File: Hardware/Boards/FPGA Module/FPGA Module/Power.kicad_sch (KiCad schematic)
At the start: 115 parts, among them Q2 IRLML6244, Q3 IRLML6244, Q4 IRLML6244, Q5 IRLML6244, Q6 IRLML6244, U10 INA700AYWFR, U12 INA700AYWFR, U13 L78L05_SOT89, U2 INA700AYWFR, U22 TPSM33625RDNR, U23 TPSM33625RDNR, U24 TPSM33625RDNR, U3 AOZ2369QI-11, U4 TPS62933O, U7 INA700AYWFR, U8 INA236

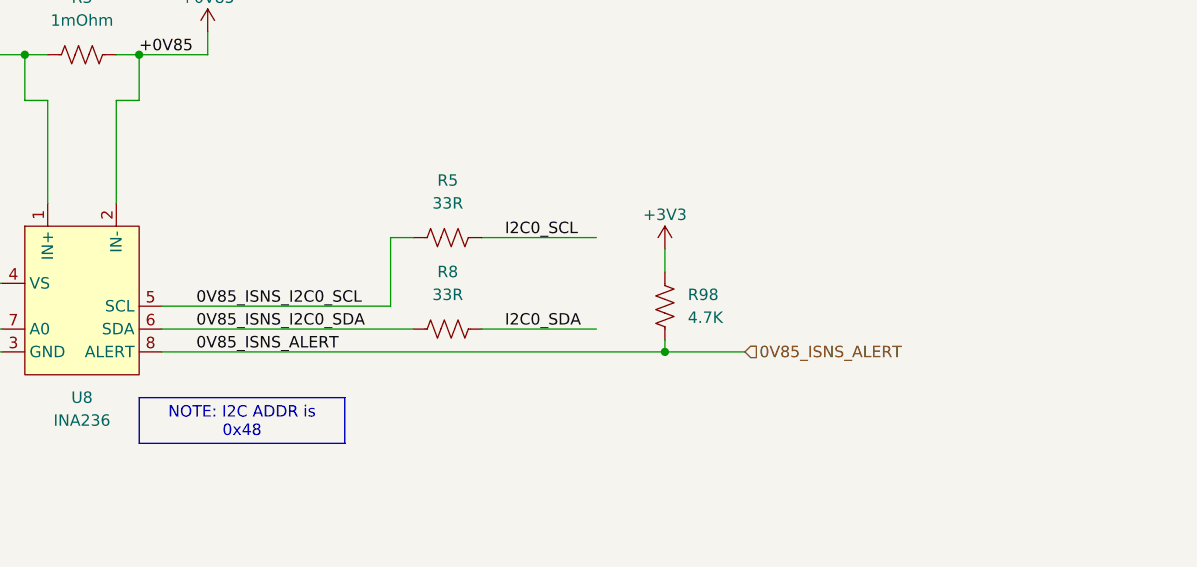
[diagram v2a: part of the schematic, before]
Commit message: Added Top sheet connections for FPGA module
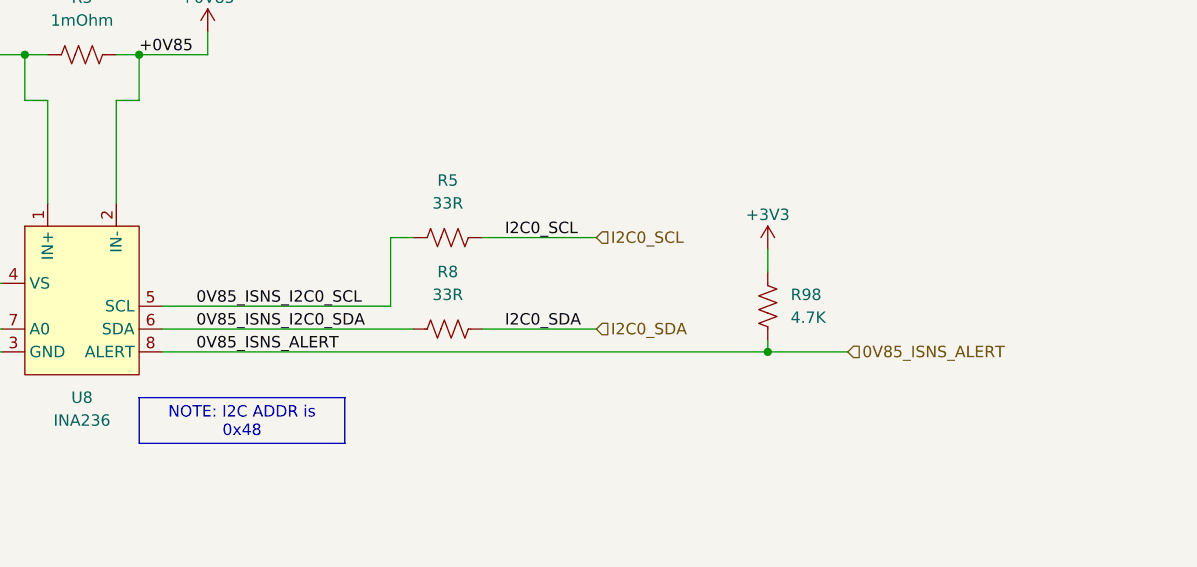
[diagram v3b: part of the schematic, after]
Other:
- moved on the sheet: R98
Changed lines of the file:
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@@
 	)
 	(junction
+		(at 375.92 74.93)
+		(diameter 0)
+		(color 0 0 0 0)
+	)
+	(junction
 		(at 210.82 331.47)
 		(diameter 0)
@@
 	)
 	(junction
-		(at 364.49 74.93)
-		(diameter 0)
-		(color 0 0 0 0)
-	)
-	(junction
 		(at 293.37 41.91)
 		(diameter 0)
@@
 	(wire
 		(pts
+			(xy 375.92 74.93) (xy 384.81 74.93)
+		)
+		(stroke
+			(width 0)
+			(type default)
+		)
+	)
+	(wire
+		(pts
 			(xy 189.23 349.25) (xy 189.23 358.14)
 		)
@@
 	(wire
 		(pts
-			(xy 308.61 74.93) (xy 364.49 74.93)
+			(xy 308.61 74.93) (xy 375.92 74.93)
 		)
 		(stroke
@@
 	(wire
 		(pts
-			(xy 364.49 63.5) (xy 364.49 66.04)
+			(xy 375.92 63.5) (xy 375.92 66.04)
 		)
 		(stroke
@@
 	(wire
 		(pts
-			(xy 364.49 73.66) (xy 364.49 74.93)
+			(xy 375.92 73.66) (xy 375.92 74.93)
 		)
 		(stroke
@@
 	(wire
 		(pts
-			(xy 364.49 74.93) (xy 373.38 74.93)
-		)
-		(stroke
-			(width 0)
-			(type default)
-		)
-	)
-	(wire
-		(pts
 			(xy 185.42 214.63) (xy 185.42 215.9)
 		)
@@
 		)
 	)
+	(hierarchical_label "I2C0_SCL"
+		(shape input)
+		(at 356.87 62.23 0)
+		(fields_autoplaced yes)
+		(effects
+			(font
+				(size 1.27 1.27)
+			)
+			(justify left)
+		)
+	)
 	(hierarchical_label "1V8_ISNS_ALERT"
 		(shape input)
@@
 		)
 	)
+	(hierarchical_label "I2C0_SDA"
+		(shape input)
+		(at 356.87 72.39 0)
+		(fields_autoplaced yes)
+		(effects
+			(font
+				(size 1.27 1.27)
+			)
+			(justify left)
+		)
+	)
 	(hierarchical_label "1V2_ISNS_ALERT"
 		(shape input)
@@
 	(hierarchical_label "0V85_ISNS_ALERT"
 		(shape input)
-		(at 373.38 74.93 0)
+		(at 384.81 74.93 0)
 		(fields_autoplaced yes)
 		(effects
@@
 	(symbol
 		(lib_id "Device:R_US")
-		(at 364.49 69.85 180)
+		(at 375.92 69.85 180)
 		(unit 1)
 		(exclude_from_sim no)
@@
 		(fields_autoplaced yes)
 		(property "Reference" "R98"
-			(at 367.03 68.5799 0)
+			(at 378.46 68.5799 0)
 			(effects
 				(font
@@
 		)
 		(property "Value" "4.7K"
-			(at 367.03 71.1199 0)
+			(at 378.46 71.1199 0)
 			(effects
 				(font
@@
 		)
 		(property "Footprint" "Resistor_SMD:R_0402_1005Metric"
-			(at 363.474 69.596 90)
+			(at 374.904 69.596 90)
 			(effects
 				(font
@@
 		)
 		(property "Datasheet" "~"
-			(at 364.49 69.85 0)
+			(at 375.92 69.85 0)
 			(effects
 				(font
@@
 		)
 		(property "Description" "Resistor, US symbol"
-			(at 364.49 69.85 0)
+			(at 375.92 69.85 0)
 			(effects
 				(font
@@
 	(symbol
 		(lib_id "power:+3V3")
-		(at 364.49 63.5 0)
+		(at 375.92 63.5 0)
 		(unit 1)
 		(exclude_from_sim no)
@@
 		(dnp no)
 		(property "Reference" "#PWR032"
-			(at 364.49 67.31 0)
+			(at 375.92 67.31 0)
 			(effects
 				(font
@@
 		)
 		(property "Value" "+3V3"
-			(at 364.49 59.69 0)
+			(at 375.92 59.69 0)
 			(effects
 				(font
@@
 		)
 		(property "Footprint" ""
-			(at 364.49 63.5 0)
+			(at 375.92 63.5 0)
 			(effects
 				(font
@@
 		)
 		(property "Datasheet" ""
-			(at 364.49 63.5 0)
+			(at 375.92 63.5 0)
 			(effects
 				(font
@@
 		)
 		(property "Description" "Power symbol creates a global label with name \"+3V3\""
-			(at 364.49 63.5 0)
+			(at 375.92 63.5 0)
 			(effects
 				(font

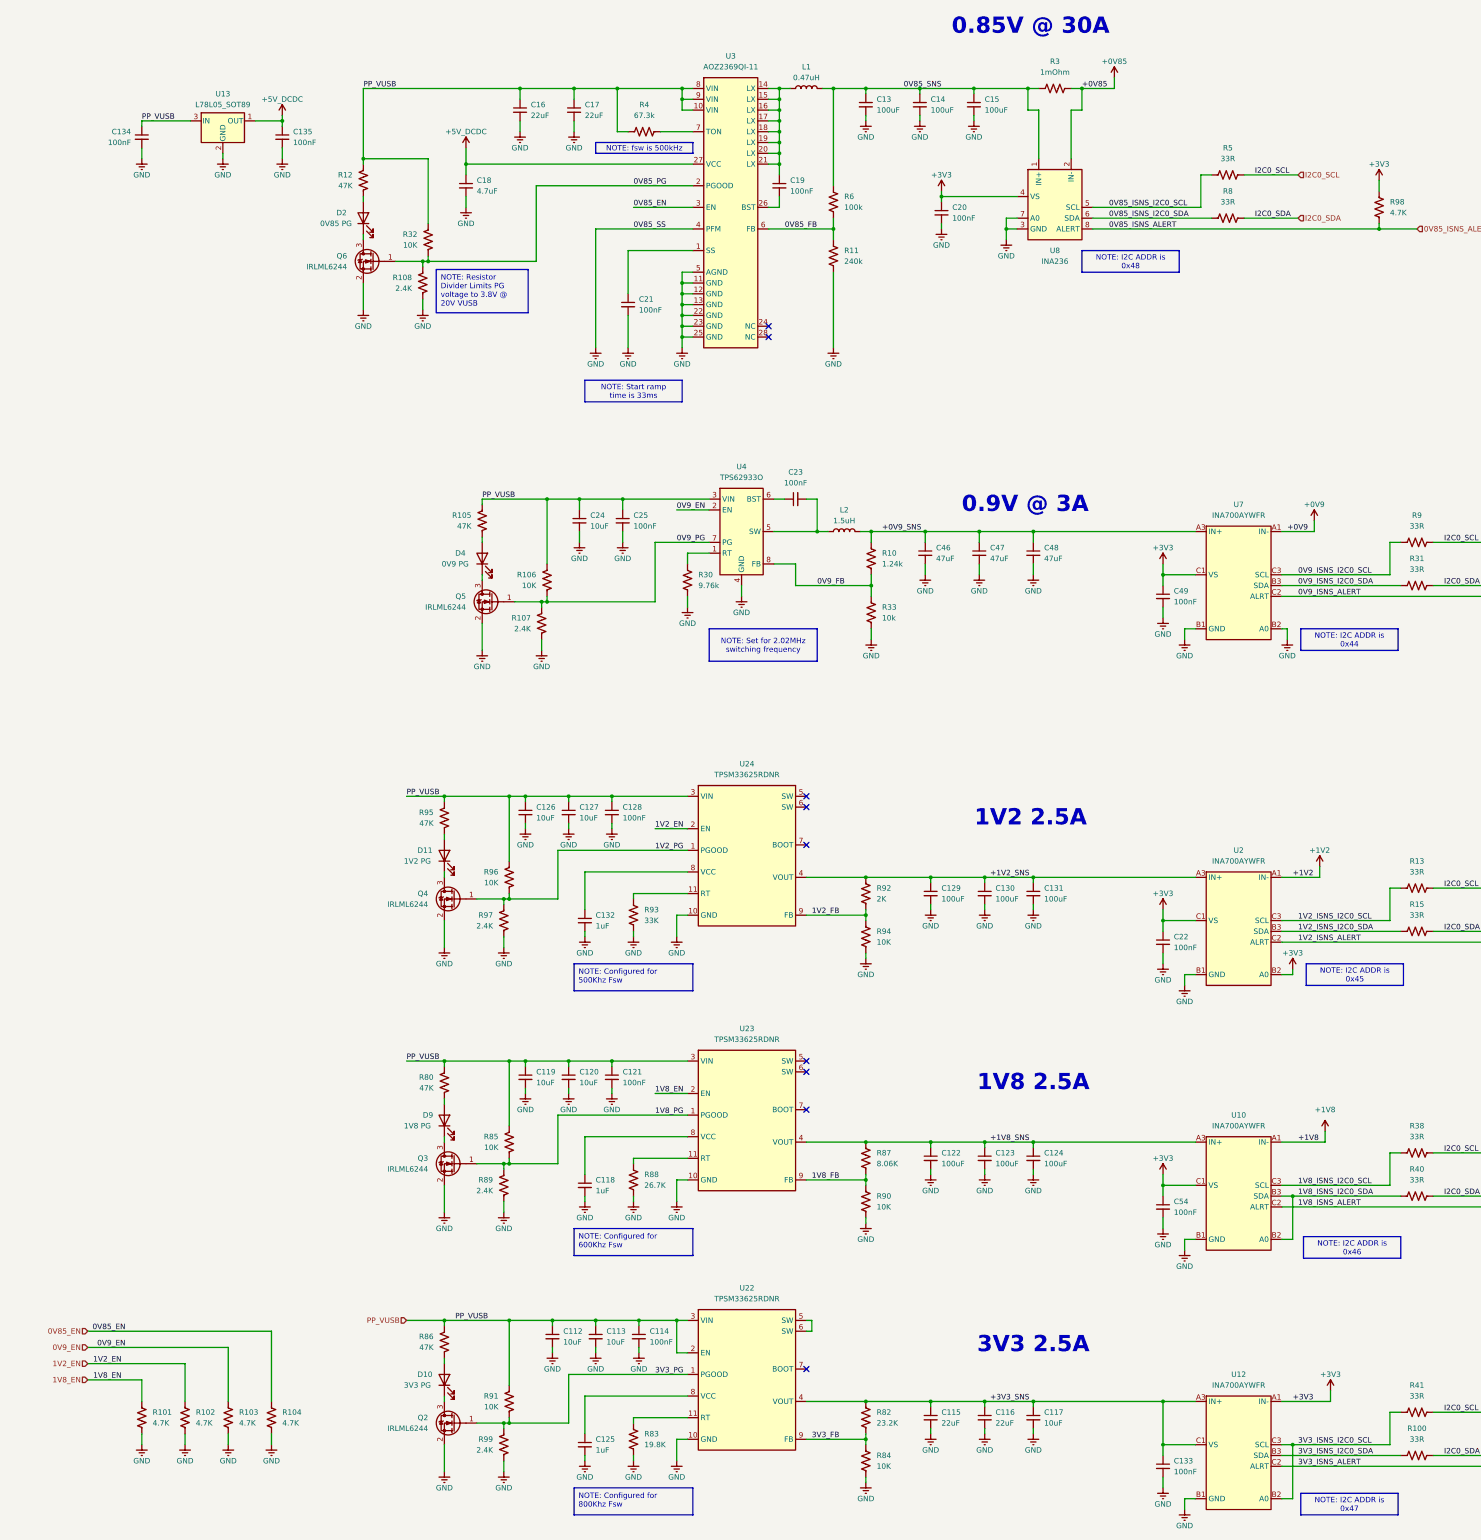
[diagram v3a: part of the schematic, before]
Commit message: FPGA Module sch update
Added 3V3 LDO for MCU and 3V3 EN for DCDC. Also added SPI bus from MCU to FPGA with level shifter
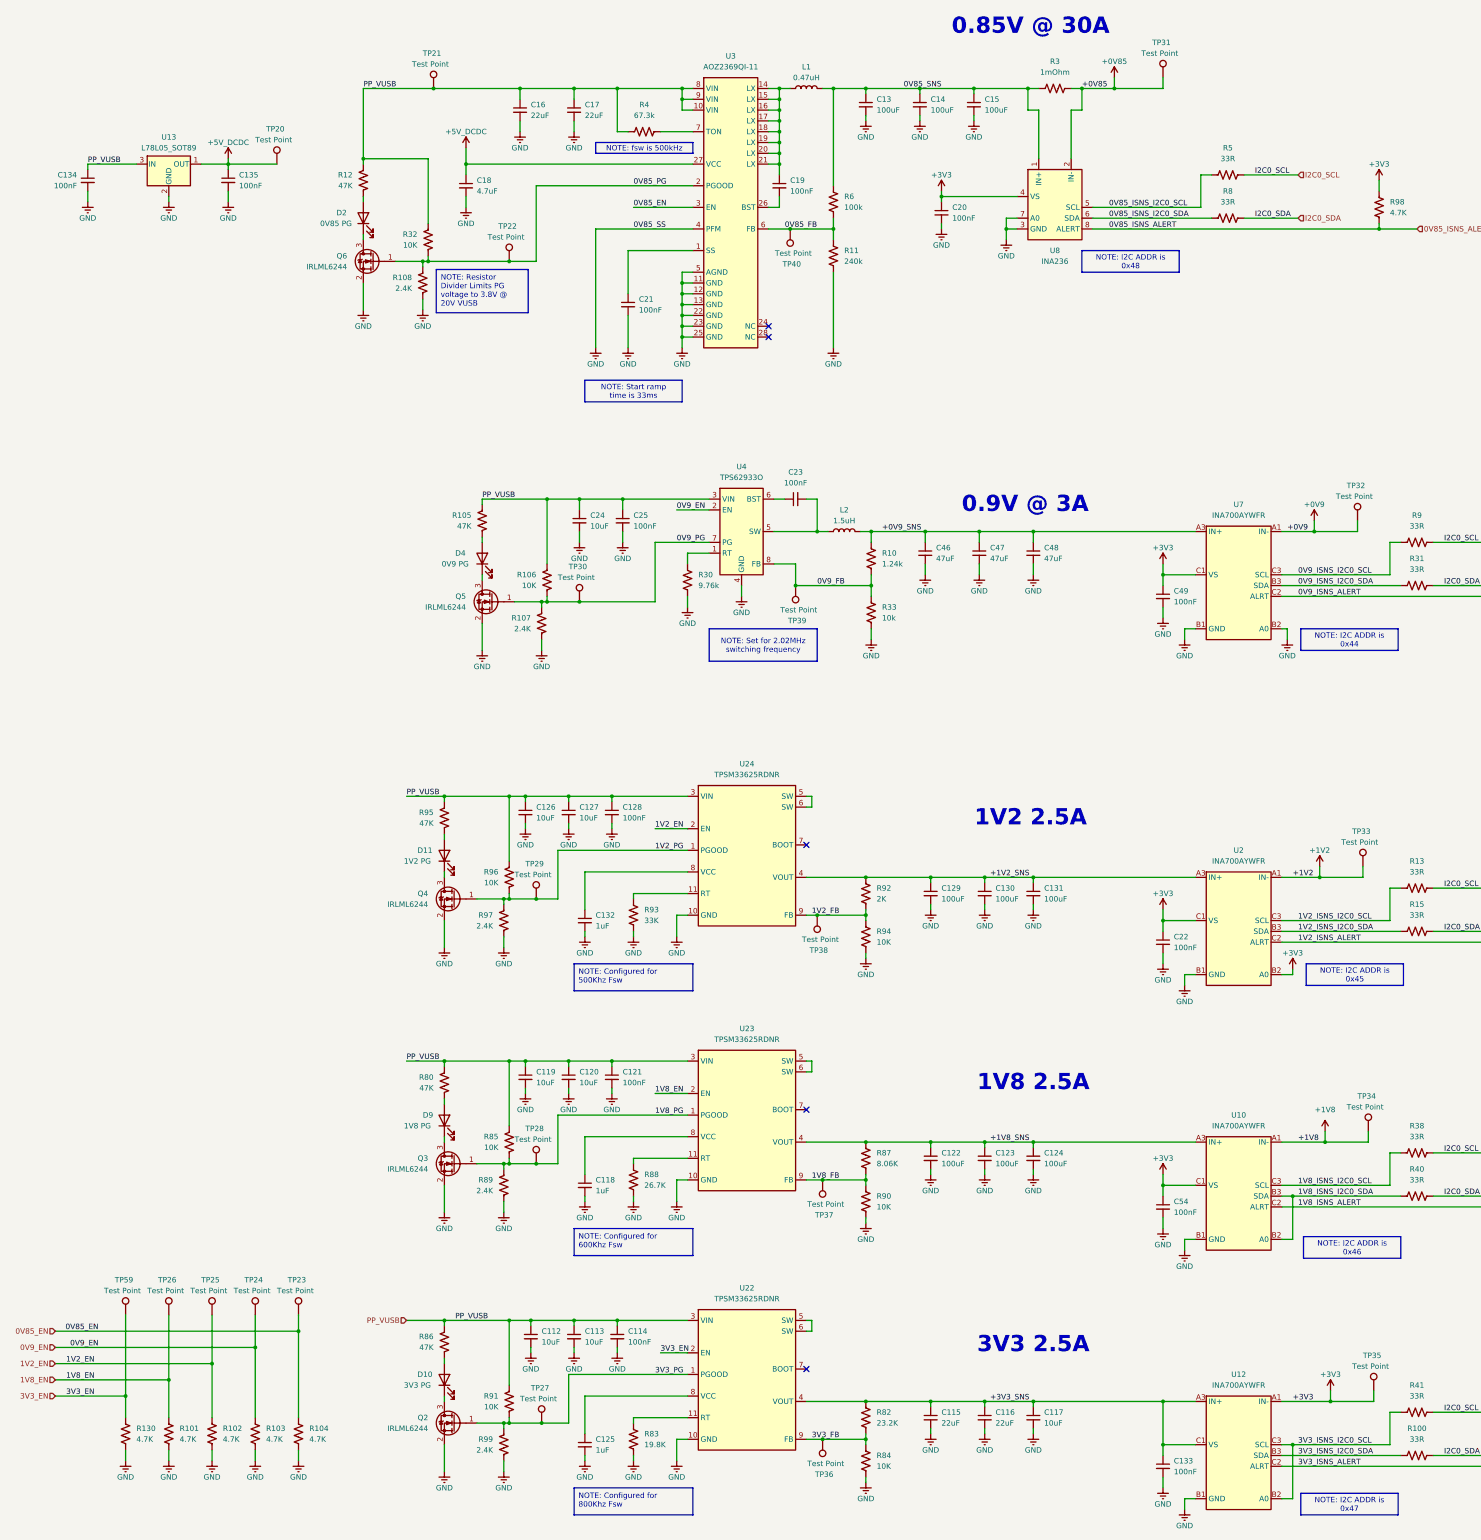
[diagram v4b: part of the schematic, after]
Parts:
- added R130: 4.7K, Resistor_SMD:R_0402_1005Metric, symbol Device:R_US
- added TP20, TP21, TP22, TP23, TP24, TP25, TP26, TP27, TP28, TP29, TP30, TP31, TP32, TP33, TP34, TP35, TP36, TP37, TP38, TP39, TP40, TP59: Test Point, FPGA Module:Test Point 0.75mm, symbol Connector:TestPoint
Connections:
- net +0V85: now also TP31.1
- net +0V9: now also TP32.1
- net +1V2: now also TP33.1
- net +1V8: now also TP34.1
- net +3V3: now also TP35.1
- net +5V_DCDC: now also TP20.1
- net 0V85_EN: now also TP23.1
- net 0V85_FB: now also TP40.1
- net 0V85_PG: now also TP22.1
- net 0V9_EN: now also TP24.1
- net 0V9_FB: now also TP39.1
- net 0V9_PG: now also TP30.1
- net 1V2_EN: now also TP25.1
- net 1V2_FB: now also TP38.1
- net 1V2_PG: now also TP29.1
- net 1V8_EN: now also TP26.1
- net 1V8_FB: now also TP37.1
- net 1V8_PG: now also TP28.1
- net 3V3_FB: now also TP36.1
- net 3V3_PG: now also TP27.1
- net GND: now also R130.1
- net PP_VUSB: now also TP21.1; no longer U22.2 (EN)
- net at U24.5 (SW): now also U24.6 (SW)
- net at U23.5 (SW): now also U23.6 (SW)
- new net 3V3_EN: R130.2, TP59.1, U22.2 (EN)
- no-connect marks 9 -> 5
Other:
- moved on the sheet: C112, C113, C114, C134, C135, R101, R102, R103, R104, U13

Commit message: Completed FPGA module PCB layout
Started PCB routing
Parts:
- removed C112, C113, C117, C119, C120, C126, C127, C24: 10uF, Capacitor_SMD:C_0603_1608Metric, symbol Device:C_Small
- removed C114, C121, C128: 100nF, Capacitor_SMD:C_0201_0603Metric, symbol Device:C_Small
- removed C115, C116, C16, C17: 22uF, Capacitor_SMD:C_0805_2012Metric, symbol Device:C_Small
- removed C118, C125, C132: 1uF, Capacitor_SMD:C_0402_1005Metric, symbol Device:C_Small
- removed C122, C123, C124, C129, C13, C130, C131, C14, C15: 100uF, Capacitor_SMD:C_0805_2012Metric, symbol Device:C_Small
- removed C134, C135, C19, C21, C23, C25: 100nF, Capacitor_SMD:C_0402_1005Metric, symbol Device:C_Small
- removed C18: 4.7uF, Capacitor_SMD:C_0402_1005Metric, symbol Device:C_Small
- removed C46, C47, C48: 47uF, Capacitor_SMD:C_0603_1608Metric, symbol Device:C_Small
- removed D2: 0V85 PG, LED_SMD:LED_0603_1608Metric, symbol Device:LED
- removed D4: 0V9 PG, LED_SMD:LED_0603_1608Metric, symbol Device:LED
- removed Q2, Q3, Q4, Q5, Q6: IRLML6244, Package_TO_SOT_SMD:SOT-23, symbol Transistor_FET:IRLML6244
- removed R10: 1.24k, Resistor_SMD:R_0402_1005Metric, symbol Device:R_US
- removed R105, R12, R80, R86, R95: 47K, Resistor_SMD:R_0402_1005Metric, symbol Device:R_US
- removed R106, R32, R84, R90, R91, R96: 10K, Resistor_SMD:R_0402_1005Metric, symbol Device:R_US
- removed R107, R108, R89, R97, R99: 2.4K, Resistor_SMD:R_0402_1005Metric, symbol Device:R_US
- removed R11: 240k, Resistor_SMD:R_0402_1005Metric, symbol Device:R_US
- removed R30: 9.76k, Resistor_SMD:R_0402_1005Metric, symbol Device:R_US
- removed R33: 10k, Resistor_SMD:R_0402_1005Metric, symbol Device:R_US
- removed R4: 67.3k, Resistor_SMD:R_0402_1005Metric, symbol Device:R_US
- removed R6: 100k, Resistor_SMD:R_0402_1005Metric, symbol Device:R_US
- removed R82: 23.2K, Resistor_SMD:R_0402_1005Metric, symbol Device:R_US
- removed R83: 19.8K, Resistor_SMD:R_0402_1005Metric, symbol Device:R_US
- removed R87: 8.06K, Resistor_SMD:R_0402_1005Metric, symbol Device:R_US
- removed R88: 26.7K, Resistor_SMD:R_0402_1005Metric, symbol Device:R_US
- removed R92: 2K, Resistor_SMD:R_0402_1005Metric, symbol Device:R_US
- removed R93: 33K, Resistor_SMD:R_0402_1005Metric, symbol Device:R_US
- removed TP20, TP21, TP22, TP27, TP28, TP29, TP30, TP36, TP37, TP38, TP39, TP40: Test Point, FPGA Module:Test Point 0.75mm, symbol Connector:TestPoint
- removed U13: L78L05_SOT89, Package_TO_SOT_SMD:SOT-89-3, symbol Regulator_Linear:L78L05_SOT89
- removed U22, U23, U24: TPSM33625RDNR, IO_Module:RDN0011A-MFG, symbol IO_Module:TPSM33625
- removed U3: AOZ2369QI-11, FPGA Module:AOZ2369QI11, symbol FPGA Module:AOZ2369QI-11
- removed U4: TPS62933O, Package_TO_SOT_SMD:SOT-583-8, symbol Regulator_Switching:TPS62933O
- added C140, C141, C142, C143: 1nF, Capacitor_SMD:C_0201_0603Metric, symbol Device:C_Small
- added C144, C145, C166, C169, C170, C171, C172, C173: 47uF, Capacitor_SMD:C_0603_1608Metric, symbol Device:C_Small
- added C146, C147, C148, C161, C162, C163, C77, C78, C79, C80, C81, C82, C83, C84: 22uF, Capacitor_SMD:C_0805_2012Metric, symbol Device:C_Small
- added C149, C164, C174, C175, C176, C177: 100nF, Capacitor_SMD:C_0201_0603Metric, symbol Device:C_Small
- added C150, C160, C165: 220nF, Capacitor_SMD:C_0201_0603Metric, symbol Device:C_Small
- added C151: 2.2nF, Capacitor_SMD:C_0402_1005Metric, symbol Device:C_Small
- added C152, C153, C154, C157: 100uF, Capacitor_SMD:C_0805_2012Metric, symbol Device:C_Small
- added C155, C156: 560uF, Capacitor_Tantalum_SMD:CP_EIA-7343-31_Kemet-D, symbol Device:C_Polarized_Small_US
- added C158, C159, C167, C168: 4.7uF, Capacitor_SMD:C_0201_0603Metric, symbol Device:C_Small
- added C178, C180, C182, C184: 4.7pF, Capacitor_SMD:C_0201_0603Metric, symbol Device:C_Small
- added C179, C181, C183, C185: 220pF, Capacitor_SMD:C_0201_0603Metric, symbol Device:C_Small
- added C186, C91: 10uF, Capacitor_SMD:C_0603_1608Metric, symbol Device:C_Small
- added C73, C85, C88, C89, C90: 1uF, Capacitor_SMD:C_0402_1005Metric, symbol Device:C_Small
- added C87, C92: 4.7uF, Capacitor_SMD:C_0402_1005Metric, symbol Device:C_Small
- added D7: 0V85 PG, LED_SMD:LED_0603_1608Metric, symbol Device:LED
- added D8: 3V3 PG, LED_SMD:LED_0603_1608Metric, symbol Device:LED
- added L3: 1uH, Inductor_SMD:L_1210_3225Metric, symbol Device:L
- added L4: 220nH, FPGA Module:IND_SRP6530A_BRN, symbol Device:L
- added L5: 560nH, FPGA Module:L_Bourns_SRP3012, symbol Device:L
- added L7: 300nH, Inductor_SMD:L_Taiyo-Yuden_MD-3030, symbol Device:L
- added R132, R138, R140, R142, R143, R144, R145, R151, R154, R155, R157, R65: 10K, Resistor_SMD:R_0201_0603Metric, symbol Device:R_US
- added R133: 20K, Resistor_SMD:R_0201_0603Metric, symbol Device:R_US
- added R134: 47K, Resistor_SMD:R_0201_0603Metric, symbol Device:R_US
- added R135, R136, R146, R149, R150, R152, R153, R161: 0R, Resistor_SMD:R_0201_0603Metric, symbol Device:R_US
- added R137, R156: 2.2R, Resistor_SMD:R_0603_1608Metric, symbol Device:R_US
- added R139: 14K, Resistor_SMD:R_0201_0603Metric, symbol Device:R_US
- added R141: 8.06K, Resistor_SMD:R_0201_0603Metric, symbol Device:R_US
- added R147, R167: 24K, Resistor_SMD:R_0201_0603Metric, symbol Device:R_US
- added R148, R168: 81K, Resistor_SMD:R_0201_0603Metric, symbol Device:R_US
- added R57, R67, R76: 4.7K, Resistor_SMD:R_0201_0603Metric, symbol Device:R_US
- added R63: 33K, Resistor_SMD:R_0201_0603Metric, symbol Device:R_US
- added R64: 56.2K, Resistor_SMD:R_0201_0603Metric, symbol Device:R_US
- added R66: 26.1K, Resistor_SMD:R_0201_0603Metric, symbol Device:R_US
- added U10: L78L33_SOT89, Package_TO_SOT_SMD:SOT-89-3, symbol Regulator_Linear:L78L33_SOT89
- added U24, U25: MP8796, FPGA Module:TQFN-4x5_MP8796B_MNP, symbol FPGA Module:MP8796GVT
- added U9: LT7200S, FPGA Module:LT7200S, symbol FPGA Module:LT7200S
- C102: renamed from C22; footprint Capacitor_SMD:C_0402_1005Metric -> Capacitor_SMD:C_0201_0603Metric
- C110: renamed from C54; footprint Capacitor_SMD:C_0402_1005Metric -> Capacitor_SMD:C_0201_0603Metric
- C118: renamed from C133; footprint Capacitor_SMD:C_0402_1005Metric -> Capacitor_SMD:C_0201_0603Metric
- C86: renamed from C20; footprint Capacitor_SMD:C_0402_1005Metric -> Capacitor_SMD:C_0201_0603Metric
- C94: renamed from C49; footprint Capacitor_SMD:C_0402_1005Metric -> Capacitor_SMD:C_0201_0603Metric
- D10: value 3V3 PG -> 1V2 PG
- D11: value 1V2 PG -> 0V9 PG
- L1: value 0.47uH -> 220nH; footprint FPGA Module:INDM135125X500N -> FPGA Module:IND_SRP6530A_BRN; MPN SRP1245A-R47M -> PA5041.221HLT
- L2: value 1.5uH -> 560nH; footprint FPGA Module:SRU1038100Y -> FPGA Module:L_Bourns_SRP3012; MPN SRU1038-1R5Y -> SRP3012TA-R56M
- R100: renamed from R102; footprint Resistor_SMD:R_0402_1005Metric -> Resistor_SMD:R_0201_0603Metric
- R101: renamed from R103; footprint Resistor_SMD:R_0402_1005Metric -> Resistor_SMD:R_0201_0603Metric
- R102: renamed from R104; footprint Resistor_SMD:R_0402_1005Metric -> Resistor_SMD:R_0201_0603Metric
- R105: renamed from R7; footprint Resistor_SMD:R_0402_1005Metric -> Resistor_SMD:R_0201_0603Metric
- R106: renamed from R100; footprint Resistor_SMD:R_0402_1005Metric -> Resistor_SMD:R_0201_0603Metric
- R56: renamed from R3; value 1mOhm -> 500uOhm
- R58: renamed from R5; footprint Resistor_SMD:R_0402_1005Metric -> Resistor_SMD:R_0201_0603Metric
- R61: renamed from R98; footprint Resistor_SMD:R_0402_1005Metric -> Resistor_SMD:R_0201_0603Metric
- R62: renamed from R8; footprint Resistor_SMD:R_0402_1005Metric -> Resistor_SMD:R_0201_0603Metric
- R68: renamed from R9; footprint Resistor_SMD:R_0402_1005Metric -> Resistor_SMD:R_0201_0603Metric
- R70: renamed from R39; footprint Resistor_SMD:R_0402_1005Metric -> Resistor_SMD:R_0201_0603Metric
- R73: renamed from R31; footprint Resistor_SMD:R_0402_1005Metric -> Resistor_SMD:R_0201_0603Metric
- R78: renamed from R13; footprint Resistor_SMD:R_0402_1005Metric -> Resistor_SMD:R_0201_0603Metric
- R82: renamed from R29; footprint Resistor_SMD:R_0402_1005Metric -> Resistor_SMD:R_0201_0603Metric
- R83: renamed from R15; footprint Resistor_SMD:R_0402_1005Metric -> Resistor_SMD:R_0201_0603Metric
- R85, R94: value 10K -> 4.7K; footprint Resistor_SMD:R_0402_1005Metric -> Resistor_SMD:R_0201_0603Metric
- R87: renamed from R38; footprint Resistor_SMD:R_0402_1005Metric -> Resistor_SMD:R_0201_0603Metric
- R91: renamed from R14; footprint Resistor_SMD:R_0402_1005Metric -> Resistor_SMD:R_0201_0603Metric
- R92: renamed from R40; footprint Resistor_SMD:R_0402_1005Metric -> Resistor_SMD:R_0201_0603Metric
- R96: renamed from R41; footprint Resistor_SMD:R_0402_1005Metric -> Resistor_SMD:R_0201_0603Metric
- R98: renamed from R130; footprint Resistor_SMD:R_0402_1005Metric -> Resistor_SMD:R_0201_0603Metric
- R99: renamed from R101; footprint Resistor_SMD:R_0402_1005Metric -> Resistor_SMD:R_0201_0603Metric
- renumbered TP31 to TP28, TP32 to TP33, TP33 to TP36, TP34 to TP39, TP59 to TP42, TP26 to TP43, TP25 to TP44, TP24 to TP45, TP23 to TP46, TP35 to TP47, U8 to U11, U7 to U13, U2 to U15, U10 to U17, U12 to U19
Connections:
- net +0V9_SNS: now also C143.1, C172.1, C173.1, L7.2, R141.2; no longer L2.2
- net +1V2_SNS: now also L2.2, C142.1, C170.1, C171.1, R139.2
- net +1V8_SNS: now also C141.1, C166.1, C169.1, L5.2, R66.2
- net +3V3_SNS: now also C140.1, C144.1, C145.1, L3.2, R64.2
- net 0V85_EN: now also U24.9 (EN), U25.9 (EN)
- net 0V85_PG: now also D7.2 (A), R57.1, U24.10 (PG), U25.10 (PG)
- net 0V85_SNS: now also C152.1, C153.1, C154.1, C155.1, C156.1, C157.1, L4.2, R135.1
- net 0V9_EN: now also U9.20 (RUN4)
- net 0V9_FB: now also C143.2, R141.1, R145.2, U9.22 (FB4)
- net 0V9_PG: now also D11.2 (A), R94.1, U9.24 (PGOOD4)
- net 1V2_EN: now also U9.43 (RUN3)
- net 1V2_FB: now also C142.2, R139.1, R140.2, U9.41 (FB3); no longer R94.2
- net 1V2_PG: now also D10.2 (A), R85.1, U9.39 (PGOOD3)
- net 1V8_EN: now also U9.44 (RUN2)
- net 1V8_FB: now also C141.2, R132.2, R66.1, U9.46 (FB2)
- net 1V8_PG: now also D9.2 (A), R76.1, U9.48 (PGOOD2); no longer R85.1
- net 3V3_EN: now also U9.19 (RUN1)
- net 3V3_FB: now also C140.2, R64.1, R65.2, U9.17 (FB1)
- net 3V3_PG: now also D8.2 (A), R67.1, U9.15 (PGOOD1)
- net GND: now also D10.1 (K), D11.1 (K), D9.1 (K), C144.2, C145.2, C146.2, C147.2, C148.2, C149.2, C152.2, C153.2, C154.2, C155.2, C156.2, C157.2, C158.2, C159.2, C160.2, C161.2, C162.2, C163.2, C164.2, C166.2, C167.2, C168.2, C169.2, C170.2, C171.2, C172.2, C173.2, C174.2, C175.2, C176.2, C177.2, C178.2, C179.2, C180.2, C181.2, C182.2, C183.2, C184.2, C185.2, C186.2, C73.2, C77.2, C78.2, C79.2, C80.2, C81.2, C82.2, C83.2, C84.2, C85.2, C87.2, C88.2, C89.2, C90.2, C91.2, C92.2, D7.1 (K), D8.1 (K), R132.1, R136.1, R140.1, R145.1, R147.1, R148.1, R150.2, R167.1, R168.1, R63.1, R65.1, U10.2 (GND), U24.14 (PGND), U24.15 (PGND), U24.23 (AGND), U24.4 (PGND), U25.14 (PGND), U25.15 (PGND), U25.23 (AGND), U25.4 (PGND), U9.1 (PHMODE), U9.12 (GND), U9.13 (GND), U9.2 (GND), U9.26 (GND), U9.27 (GND), U9.3 (GND), U9.36 (GND), U9.37 (GND), U9.49 (EPAD); no longer R94.1
- net PP_VUSB: now also C146.1, C147.1, C148.1, C149.1, C161.1, C162.1, C163.1, C164.1, C186.1, C73.1, C77.1, C78.1, C79.1, C80.1, C81.1, C82.1, C83.1, C84.1, C85.1, C88.1, C89.1, C90.1, U10.3 (IN), U24.1 (VIN), U24.16 (VIN), U25.1 (VIN), U25.16 (VIN), U9.10 (SVIN), U9.11 (PVIN1), U9.28 (PVIN4), U9.29 (PVIN4), U9.34 (PVIN3), U9.35 (PVIN3), U9.4 (PVIN2), U9.5 (PVIN2); no longer R85.2
- net 1V2_LX: now reaches L2.1
- net 1V2_LX: now also U9.32 (SW3), U9.33 (SW3)
- net VCORE_LX1: now reaches L1.1
- net VCORE_LX1: now also C150.1, U24.2 (SW), U24.3 (SW)
- new net: C180.1, R154.2, U9.45 (ITH2)
- new net: R63.2, U9.38 (RT)
- new net: R161.2, U25.11 (PASS)
- new net: C181.1, R154.1
- new net: R168.2, U25.20 (ILIM)
- new net: C150.2, U24.25 (BST)
- new net: R146.1, R150.1, U9.14 (MODE/SYNC)
- new net: C175.1, U9.47 (TRACK2)
- new net: R167.2, U25.17 (FREQ)
- new net: C179.1, R151.1
- new net: C178.1, R151.2, U9.18 (ITH1)
- new net: C165.2, U25.25 (BST)
- new net: C174.1, U9.16 (TRACK1)
- new net: C184.1, R157.2, U9.21 (ITH4)
- new net: C177.1, U9.23 (TRACK4)
- new net: C176.1, U9.40 (TRACK3)
- new net: C182.1, R155.2, U9.42 (ITH3)
- new net: C185.1, R157.1
- new net: R152.2, U24.13 (SET)
- new net: R149.2, U24.11 (PASS)
- new net: R147.2, U24.17 (FREQ)
- new net: C160.1, U24.18 (SS)
- new net: R153.2, U24.19 (ISUM)
- new net: R148.2, U24.20 (ILIM)
- new net: C183.1, R155.1
- new net 0V85_SNS_N: R134.1, R136.2, U24.21 (RGND), U25.21 (RGND)
- new net 0V85_SNS_P: C151.1, R133.2, R135.2
- new net 0V9_LX: L7.1, U9.30 (SW4), U9.31 (SW4)
- new net 1V8_LX: L5.1, U9.6 (SW2), U9.7 (SW2)
- new net 3V3_AON: C91.1, R57.2, R67.2, R76.2, R85.2, R94.2, U10.1 (OUT)
- new net 3V3_LX: L3.1, U9.8 (SW1), U9.9 (SW1)
- new net INTVCC: C87.1, C92.1, R146.2, U9.25 (INTVCC)
- new net ISUM: R153.1, U25.19 (ISUM)
- new net PASS_1: R149.1, U25.12 (TAKE)
- new net SET: R152.1, U25.13 (SET)
- new net VCORE_LX2: C165.1, L4.1, U25.2 (SW), U25.3 (SW)
- new net VCORE_VCC: C158.1, C167.1, R137.2, R138.2, R142.2, R143.2, R144.2, R156.2, U24.24 (VCC), U25.24 (VCC)
- new net VCORE_VFB: C151.2, R133.1, R134.2, U24.22 (FB), U25.22 (FB)
- new net VCORE_VRDV1: C159.1, R137.1, U24.5 (VDRV)
- new net VCORE_VRDV2: C168.1, R156.1, U25.5 (VDRV)
- new net VMODE: R144.1, U24.8 (MODE), U25.8 (MODE)
- new net VPMODE: R143.1, U24.7 (PMODE), U25.7 (PMODE)
- new net VRAMP: R142.1, U24.6 (RAMP), U25.6 (RAMP)
- new net VTAKE: R138.1, R161.1, U24.12 (TAKE)
- no-connect marks 5 -> 1
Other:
- note added: "0.85V @ 40A"
- note added: "0V9 3A"
- note added: "1V2 3A"
- note added: "1V8 3A"
- note added: "3V3 3A"
- note removed: "0.85V @ 30A"
- note removed: "0.9V @ 3A"
- note removed: "1V2 2.5A"
- note removed: "1V8 2.5A"
- note removed: "3V3 2.5A"
- moved on the sheet: C102, C110, C118, C86, C94, R100, R101, R102, R105, R106, R56, R58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
